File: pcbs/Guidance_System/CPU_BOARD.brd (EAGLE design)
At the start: 100 x 52.1 mm, 32 parts, among them J1 22-27-2081-08, J10 22-27-2081-08, J11 22-27-2081-08, J12 22-27-2081-08, J13 22-27-2081-08, J14 22-27-2081-08, J15 22-27-2041-04, J16 22-27-2041-04, J17 22-27-2021-02, J2 22-27-2021-02, J3 22-27-2041-04, J4 22-27-2041-04, J5 22-27-2081-08, J6 22-27-2021-02, J7 22-27-2081-08, J8 22-27-2021-02, J9 22-27-2021-02

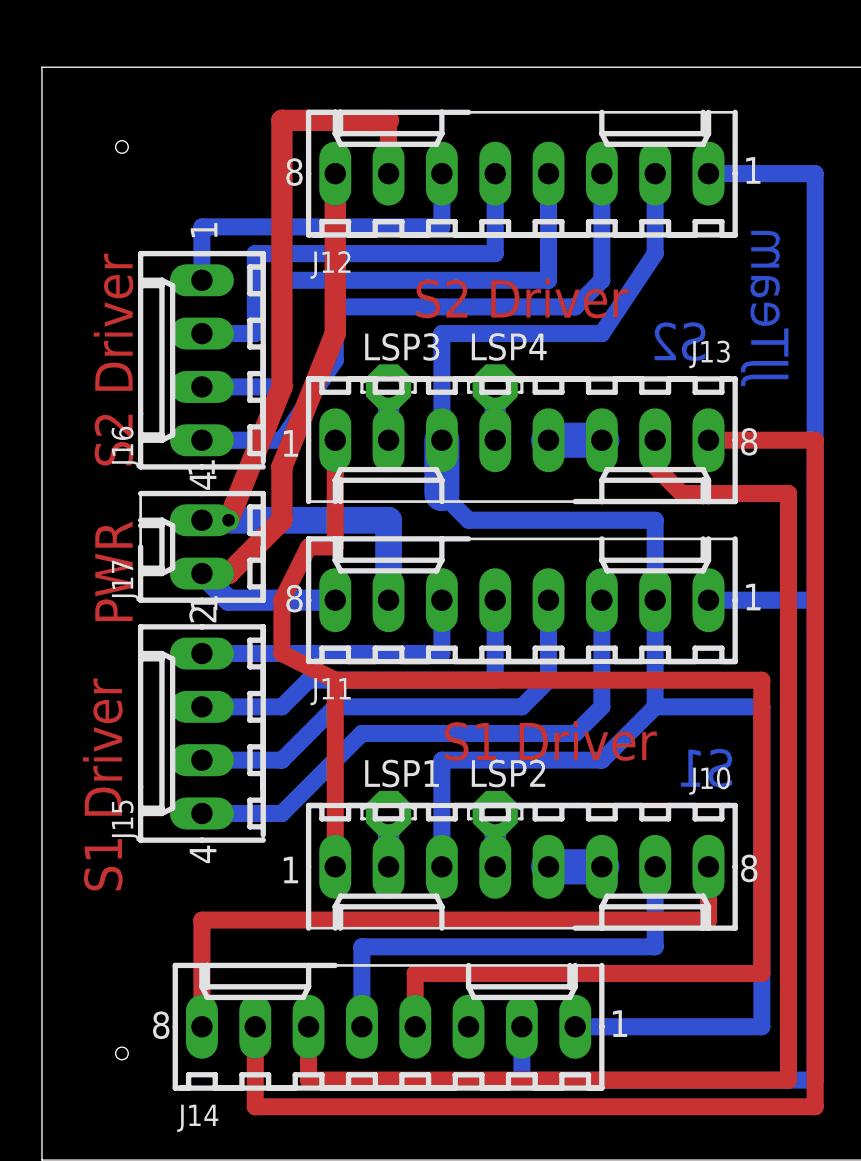
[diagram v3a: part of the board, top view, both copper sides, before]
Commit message: * Added in capacitor
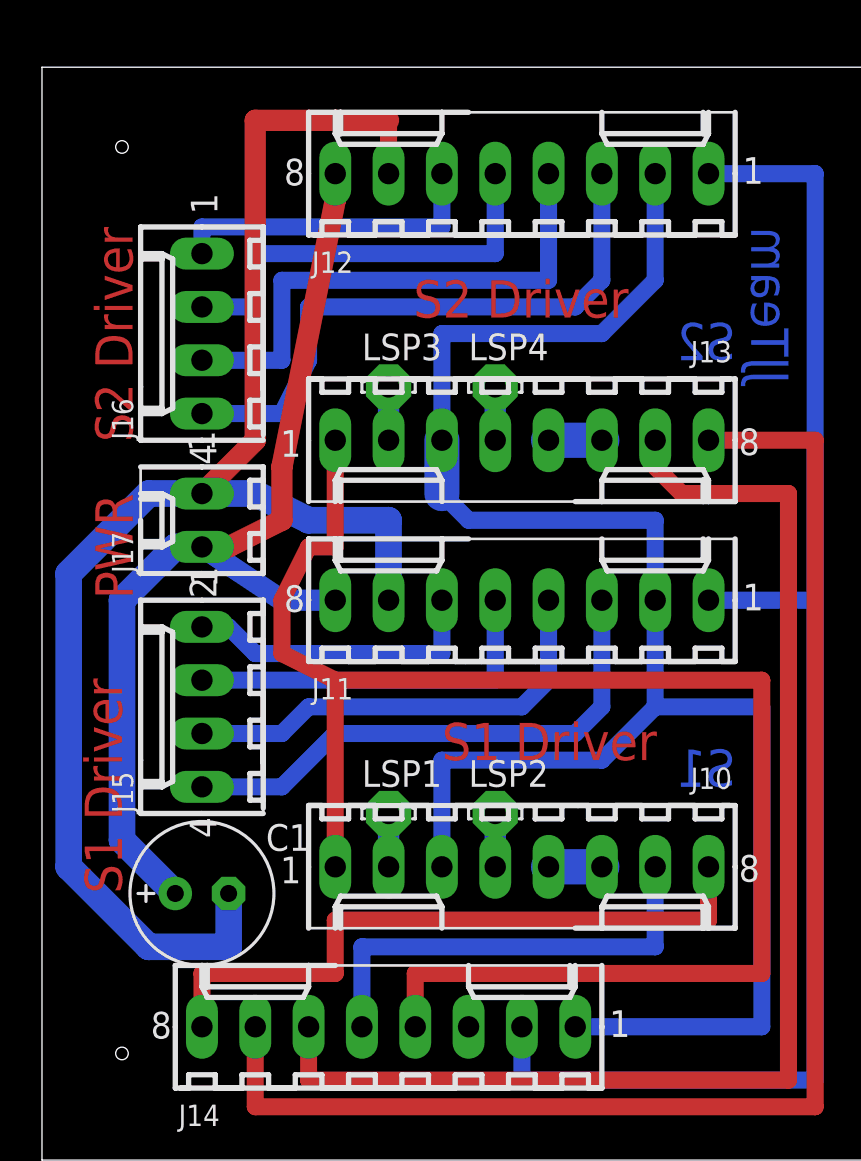
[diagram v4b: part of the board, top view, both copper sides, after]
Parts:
- added C1: (no value), resistor:E2,5-7
- moved J15 1.27 mm to (7.62, 47.0)
- moved J17 1.27 mm to (7.62, 55.9)
- moved J16 1.27 mm to (7.62, 64.8)
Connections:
- net N$31: now also C1.+
- net N$34: now also C1.-
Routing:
- net N$34: track 39.9 -> 74.4 mm, vias 1 -> 0
- net N$31: track 28.7 -> 47.9 mm
- net N$42: track 21.6 -> 20.3 mm
- net N$43: track 26.7 -> 25.4 mm
- net N$41: track 16.5 -> 15.2 mm
- net N$40: track 26.2 -> 25.7 mm
- net N$38: track 18.3 -> 17.8 mm
- net N$37: track 14.0 -> 14.5 mm
- net N$39: track 21.9 -> 21.4 mm

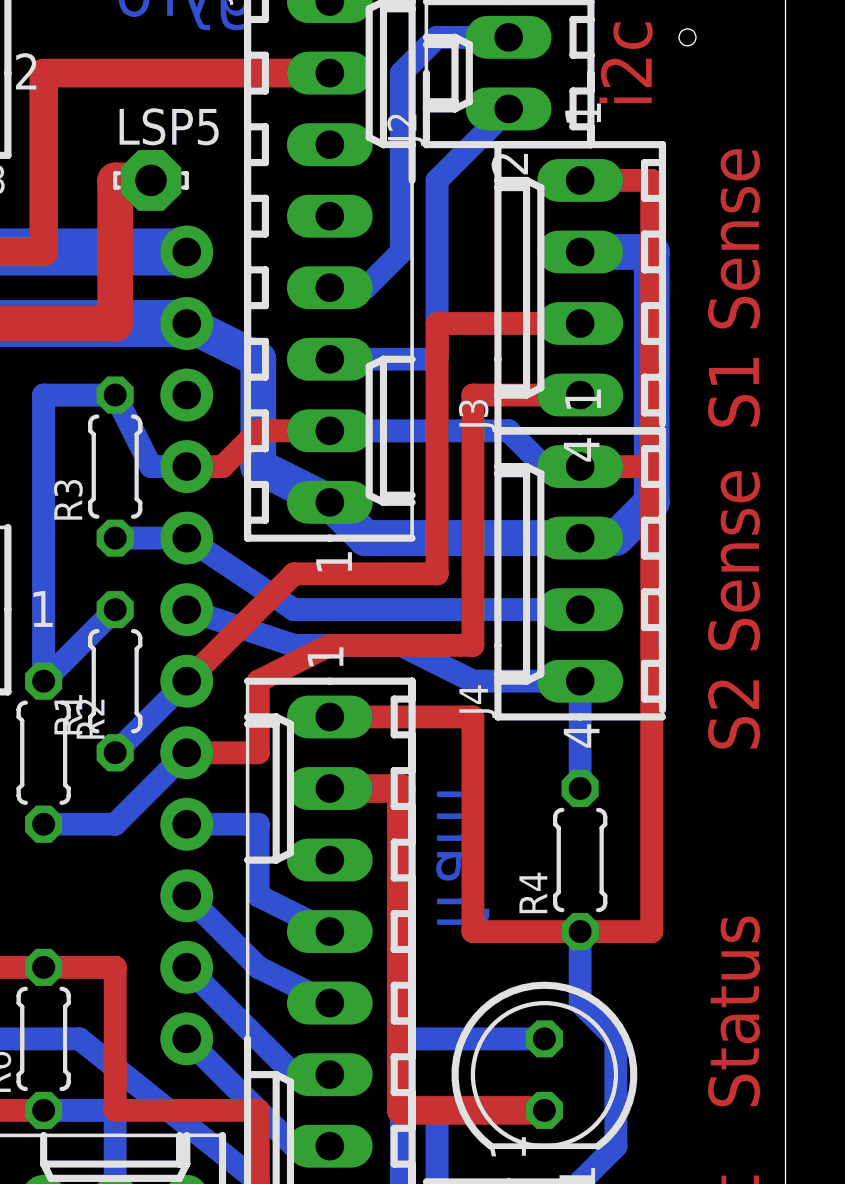
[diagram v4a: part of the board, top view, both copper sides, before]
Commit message: * Moving sensor connectors a bit further apart.
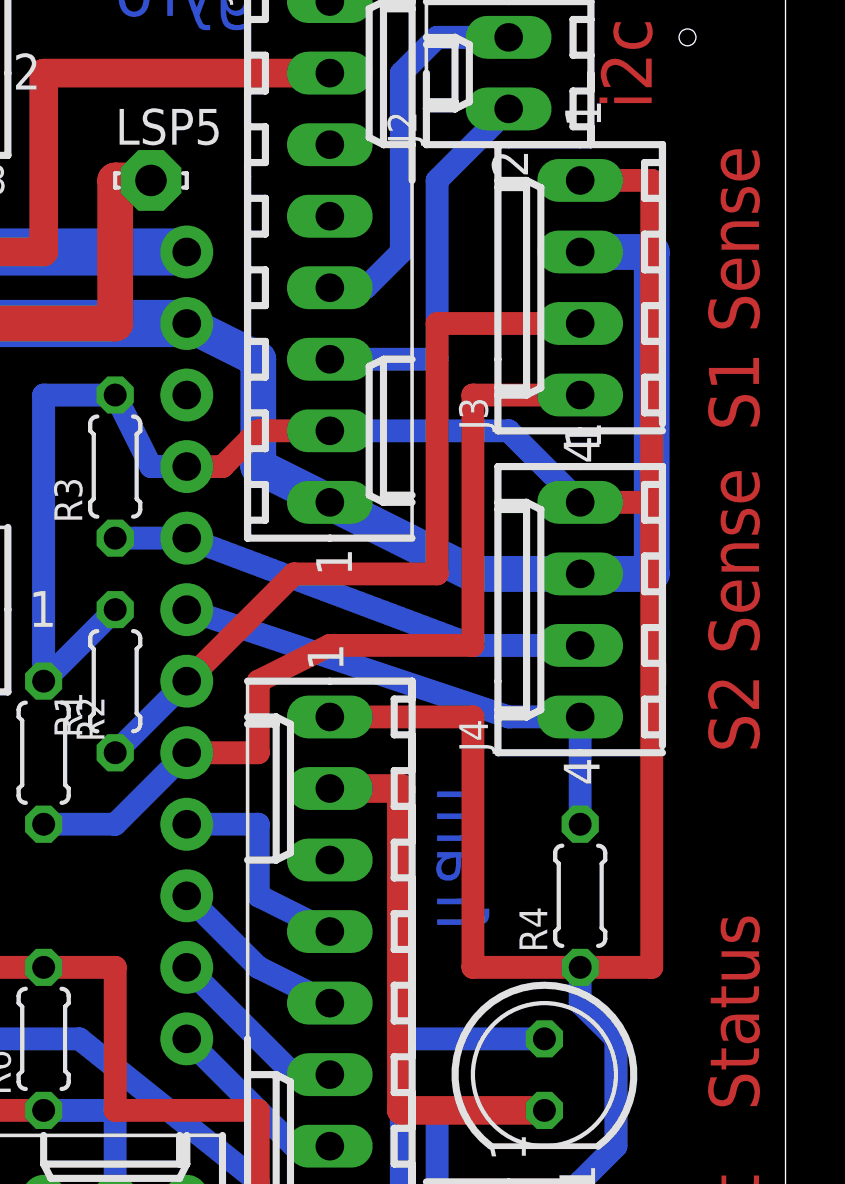
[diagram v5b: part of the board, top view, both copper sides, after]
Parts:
- moved R4 1.27 mm to (92.7, 43.2)
- moved J4 1.27 mm to (92.7, 53.3)
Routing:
- net N$24: track 53.7 -> 55.8 mm
- net N$3: track 120.3 -> 120.8 mm
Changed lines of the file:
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@@
 <attribute name="OC_FARNELL" value="unknown" x="92.71" y="64.77" size="1.778" layer="27" rot="R90" display="off"/>
 </element>
-<element name="J4" library="con-molex" package="6410-04" value="22-27-2041-04" x="92.71" y="54.61" rot="R90">
-<attribute name="MPN" value="" x="92.71" y="54.61" size="1.778" layer="27" rot="R90" display="off"/>
-<attribute name="OC_NEWARK" value="unknown" x="92.71" y="54.61" size="1.778" layer="27" rot="R90" display="off"/>
-<attribute name="MF" value="" x="92.71" y="54.61" size="1.778" layer="27" rot="R90" display="off"/>
-<attribute name="OC_FARNELL" value="unknown" x="92.71" y="54.61" size="1.778" layer="27" rot="R90" display="off"/>
+<element name="J4" library="con-molex" package="6410-04" value="22-27-2041-04" x="92.71" y="53.34" rot="R90">
+<attribute name="MPN" value="" x="92.71" y="53.34" size="1.778" layer="27" rot="R90" display="off"/>
+<attribute name="OC_NEWARK" value="unknown" x="92.71" y="53.34" size="1.778" layer="27" rot="R90" display="off"/>
+<attribute name="MF" value="" x="92.71" y="53.34" size="1.778" layer="27" rot="R90" display="off"/>
+<attribute name="OC_FARNELL" value="unknown" x="92.71" y="53.34" size="1.778" layer="27" rot="R90" display="off"/>
 </element>
 <element name="J5" library="con-molex" package="6410-08" value="22-27-2081-08" x="83.82" y="40.64" rot="R90">
@@
 <element name="R2" library="rcl" package="0204/5" value="" x="73.66" y="48.26" rot="R270"/>
 <element name="R3" library="rcl" package="0204/5" value="" x="76.2" y="58.42" rot="R90"/>
-<element name="R4" library="rcl" package="0204/5" value="" x="92.71" y="44.45" rot="R90"/>
+<element name="R4" library="rcl" package="0204/5" value="" x="92.71" y="43.18" rot="R90"/>
 <element name="R5" library="resistor" package="0204/5" value="" x="68.58" y="43.18" rot="R180"/>
 <element name="R6" library="rcl" package="0204/5" value="" x="73.66" y="38.1" rot="R90"/>
@@
 <wire x1="73.66" y1="60.96" x2="76.2" y2="60.96" width="0.8128" layer="16"/>
 <wire x1="76.2" y1="53.34" x2="73.66" y2="50.8" width="0.8128" layer="16"/>
-<wire x1="92.71" y1="41.91" x2="92.71" y2="39.37" width="0.8128" layer="16"/>
+<wire x1="92.71" y1="40.64" x2="92.71" y2="39.37" width="0.8128" layer="16"/>
 <wire x1="92.71" y1="39.37" x2="93.98" y2="38.1" width="0.8128" layer="16"/>
 <wire x1="93.98" y1="38.1" x2="93.98" y2="34.29" width="0.8128" layer="16"/>
@@
 <wire x1="92.71" y1="29.21" x2="90.17" y2="29.21" width="0.8128" layer="16"/>
 <via x="83.82" y="59.69" extent="1-16" drill="0.6" shape="square"/>
-<via x="92.71" y="58.42" extent="1-16" drill="0.6" shape="square"/>
+<via x="92.71" y="57.15" extent="1-16" drill="0.6" shape="square"/>
 <wire x1="78.74" y1="31.75" x2="78.74" y2="27.94" width="0.8128" layer="1"/>
 <wire x1="78.74" y1="27.94" x2="90.17" y2="27.94" width="0.8128" layer="1"/>
 <wire x1="90.17" y1="27.94" x2="90.17" y2="29.21" width="0.8128" layer="1"/>
 <wire x1="83.82" y1="49.53" x2="88.9" y2="49.53" width="0.8128" layer="1"/>
-<wire x1="88.9" y1="49.53" x2="88.9" y2="41.91" width="0.8128" layer="1"/>
-<wire x1="88.9" y1="41.91" x2="92.71" y2="41.91" width="0.8128" layer="1"/>
+<wire x1="88.9" y1="49.53" x2="88.9" y2="40.64" width="0.8128" layer="1"/>
+<wire x1="88.9" y1="40.64" x2="92.71" y2="40.64" width="0.8128" layer="1"/>
 <wire x1="78.74" y1="58.42" x2="80.01" y2="58.42" width="0.8128" layer="1"/>
 <wire x1="80.01" y1="58.42" x2="81.28" y2="59.69" width="0.8128" layer="1"/>
 <wire x1="81.28" y1="59.69" x2="83.82" y2="59.69" width="0.8128" layer="1"/>
-<wire x1="91.44" y1="58.42" x2="92.71" y2="58.42" width="0.4064" layer="1"/>
-<wire x1="92.71" y1="58.42" x2="95.25" y2="58.42" width="0.8128" layer="1"/>
-<wire x1="95.25" y1="58.42" x2="95.25" y2="41.91" width="0.8128" layer="1"/>
-<wire x1="95.25" y1="41.91" x2="92.71" y2="41.91" width="0.8128" layer="1"/>
+<wire x1="92.71" y1="57.15" x2="95.25" y2="57.15" width="0.8128" layer="1"/>
+<wire x1="95.25" y1="57.15" x2="95.25" y2="40.64" width="0.8128" layer="1"/>
+<wire x1="95.25" y1="40.64" x2="92.71" y2="40.64" width="0.8128" layer="1"/>
 <wire x1="92.71" y1="68.58" x2="95.25" y2="68.58" width="0.8128" layer="1"/>
-<wire x1="95.25" y1="68.58" x2="95.25" y2="58.42" width="0.8128" layer="1"/>
+<wire x1="95.25" y1="68.58" x2="95.25" y2="57.15" width="0.8128" layer="1"/>
 <wire x1="83.82" y1="59.69" x2="90.17" y2="59.69" width="0.8128" layer="16"/>
-<wire x1="90.17" y1="59.69" x2="91.44" y2="58.42" width="0.8128" layer="16"/>
-<wire x1="91.44" y1="58.42" x2="92.71" y2="58.42" width="0.8128" layer="16"/>
+<wire x1="90.17" y1="59.69" x2="92.71" y2="57.15" width="0.8128" layer="16"/>
 </signal>
 <signal name="N$5">
@@
 <contactref element="J4" pad="3"/>
 <contactref element="R3" pad="1"/>
-<wire x1="92.71" y1="53.34" x2="82.55" y2="53.34" width="0.8128" layer="16"/>
-<wire x1="82.55" y1="53.34" x2="78.74" y2="55.88" width="0.8128" layer="16"/>
+<wire x1="92.71" y1="52.07" x2="88.9" y2="52.07" width="0.8128" layer="16"/>
+<wire x1="88.9" y1="52.07" x2="78.74" y2="55.88" width="0.8128" layer="16"/>
 <wire x1="78.74" y1="55.88" x2="76.2" y2="55.88" width="0.8128" layer="16"/>
 </signal>
@@
 <contactref element="U$1" pad="19"/>
 <contactref element="R4" pad="2"/>
-<wire x1="92.71" y1="50.8" x2="92.71" y2="46.99" width="0.8128" layer="16"/>
-<wire x1="92.71" y1="50.8" x2="88.9" y2="50.8" width="0.8128" layer="16"/>
-<wire x1="88.9" y1="50.8" x2="86.36" y2="52.07" width="0.8128" layer="16"/>
-<wire x1="86.36" y1="52.07" x2="82.55" y2="52.07" width="0.8128" layer="16"/>
-<wire x1="82.55" y1="52.07" x2="78.74" y2="53.34" width="0.8128" layer="16"/>
+<wire x1="92.71" y1="49.53" x2="92.71" y2="45.72" width="0.8128" layer="16"/>
+<wire x1="92.71" y1="49.53" x2="90.17" y2="49.53" width="0.8128" layer="16"/>
+<wire x1="90.17" y1="49.53" x2="78.74" y2="53.34" width="0.8128" layer="16"/>
 </signal>
 <signal name="N$11">
@@
 <contactref element="J3" pad="2"/>
 <wire x1="92.71" y1="66.04" x2="95.25" y2="66.04" width="1.27" layer="16"/>
-<wire x1="95.25" y1="66.04" x2="95.25" y2="57.15" width="1.27" layer="16"/>
-<wire x1="95.25" y1="57.15" x2="93.98" y2="55.88" width="1.27" layer="16"/>
-<wire x1="93.98" y1="55.88" x2="92.71" y2="55.88" width="0.8128" layer="16"/>
-<wire x1="92.71" y1="55.88" x2="85.09" y2="55.88" width="1.27" layer="16"/>
-<wire x1="85.09" y1="55.88" x2="83.82" y2="57.15" width="1.27" layer="16"/>
+<wire x1="95.25" y1="66.04" x2="95.25" y2="54.61" width="1.27" layer="16"/>
+<wire x1="95.25" y1="54.61" x2="92.71" y2="54.61" width="1.27" layer="16"/>
+<wire x1="92.71" y1="54.61" x2="88.9" y2="54.61" width="1.27" layer="16"/>
+<wire x1="88.9" y1="54.61" x2="83.82" y2="57.15" width="1.27" layer="16"/>
 <wire x1="71.12" y1="53.34" x2="71.12" y2="57.15" width="1.6764" layer="16"/>
 <wire x1="71.12" y1="57.15" x2="71.12" y2="63.5" width="1.6764" layer="16"/>
